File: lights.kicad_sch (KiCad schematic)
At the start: 0 parts

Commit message: Add Neopix
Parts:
- added C?: 1000uF, symbol Device:C
- added D? (x60): SK6812, LED_SMD:LED_SK6812_PLCC4_5.0x5.0mm_P3.2mm, symbol LED:SK6812
- added IC?: 74AHCT1G125DBVRG4, SOT95P280X145-5N, symbol JonasLib-Git:74AHCT1G125DBVRG4
- added R?: 100, symbol Device:R
- added R?: 470, symbol Device:R
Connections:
- new net: D?.2 (DIN), D?.4 (DOUT) (x59)
- new net: IC?.2 (A), R?.2
- new net: IC?.4 (Y), R?.1
- new net: D?.2 (DIN), R?.2
- new net GND: C?.2, D?.1 (VSS), D?.1 (VSS), D?.1 (VSS), D?.1 (VSS), D?.1 (VSS), D?.1 (VSS), D?.1 (VSS), D?.1 (VSS), D?.1 (VSS), D?.1 (VSS), D?.1 (VSS), D?.1 (VSS), D?.1 (VSS), D?.1 (VSS), D?.1 (VSS), D?.1 (VSS), D?.1 (VSS), D?.1 (VSS), D?.1 (VSS), D?.1 (VSS), D?.1 (VSS), D?.1 (VSS), D?.1 (VSS), D?.1 (VSS), D?.1 (VSS), D?.1 (VSS), D?.1 (VSS), D?.1 (VSS), D?.1 (VSS), D?.1 (VSS), D?.1 (VSS), D?.1 (VSS), D?.1 (VSS), D?.1 (VSS), D?.1 (VSS), D?.1 (VSS), D?.1 (VSS), D?.1 (VSS), D?.1 (VSS), D?.1 (VSS), D?.1 (VSS), D?.1 (VSS), D?.1 (VSS), D?.1 (VSS), D?.1 (VSS), D?.1 (VSS), D?.1 (VSS), D?.1 (VSS), D?.1 (VSS), D?.1 (VSS), D?.1 (VSS), D?.1 (VSS), D?.1 (VSS), D?.1 (VSS), D?.1 (VSS), D?.1 (VSS), D?.1 (VSS), D?.1 (VSS), D?.1 (VSS), D?.1 (VSS), IC?.1 (~{OE}), IC?.3 (GND)
- new net PC13: R?.1
- new net VBUS: C?.1, D?.3 (VDD), D?.3 (VDD), D?.3 (VDD), D?.3 (VDD), D?.3 (VDD), D?.3 (VDD), D?.3 (VDD), D?.3 (VDD), D?.3 (VDD), D?.3 (VDD), D?.3 (VDD), D?.3 (VDD), D?.3 (VDD), D?.3 (VDD), D?.3 (VDD), D?.3 (VDD), D?.3 (VDD), D?.3 (VDD), D?.3 (VDD), D?.3 (VDD), D?.3 (VDD), D?.3 (VDD), D?.3 (VDD), D?.3 (VDD), D?.3 (VDD), D?.3 (VDD), D?.3 (VDD), D?.3 (VDD), D?.3 (VDD), D?.3 (VDD), D?.3 (VDD), D?.3 (VDD), D?.3 (VDD), D?.3 (VDD), D?.3 (VDD), D?.3 (VDD), D?.3 (VDD), D?.3 (VDD), D?.3 (VDD), D?.3 (VDD), D?.3 (VDD), D?.3 (VDD), D?.3 (VDD), D?.3 (VDD), D?.3 (VDD), D?.3 (VDD), D?.3 (VDD), D?.3 (VDD), D?.3 (VDD), D?.3 (VDD), D?.3 (VDD), D?.3 (VDD), D?.3 (VDD), D?.3 (VDD), D?.3 (VDD), D?.3 (VDD), D?.3 (VDD), D?.3 (VDD), D?.3 (VDD), D?.3 (VDD), IC?.5 (VCC)

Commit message: Finalilize the Keybord Shematic
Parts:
- added D? (x2): SK6812, LED_SMD:LED_SK6812_PLCC4_5.0x5.0mm_P3.2mm, symbol LED:SK6812
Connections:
- net GND: now also D?.1 (VSS), D?.1 (VSS)
- net VBUS: now also D?.3 (VDD), D?.3 (VDD)
- net at D?.4 (DOUT): now also D?.2 (DIN)
- net PC13 renamed PA0
- new net: D?.2 (DIN), D?.4 (DOUT)
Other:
- note added: "62 Neopix - USB.2.0 Device max 6.40 mA per NeoPix ~ 10% Brightness"

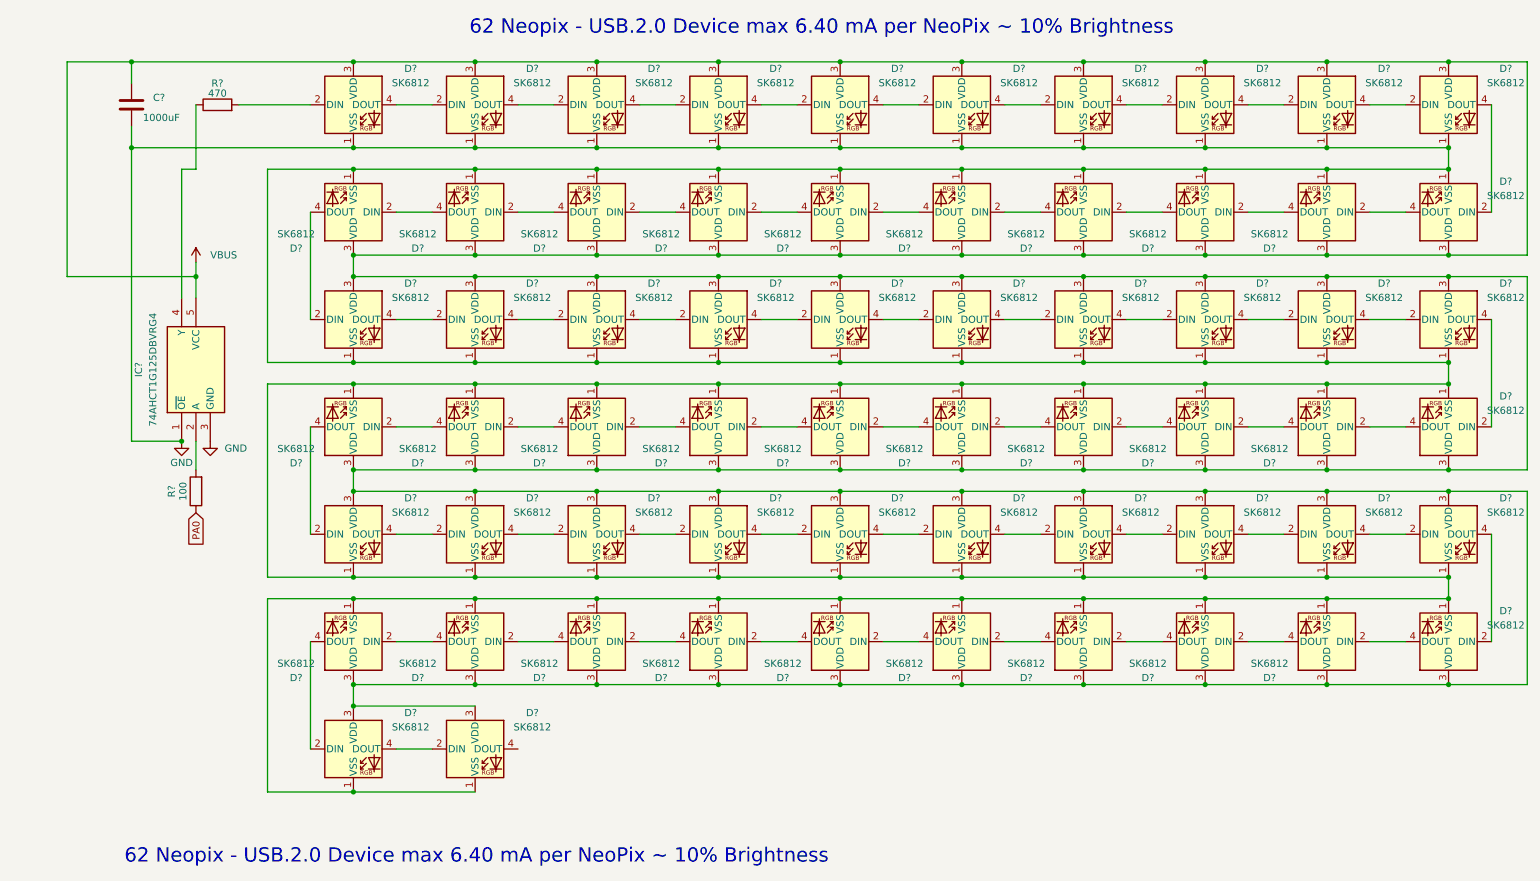
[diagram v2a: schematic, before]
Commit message: Start to fix ERC
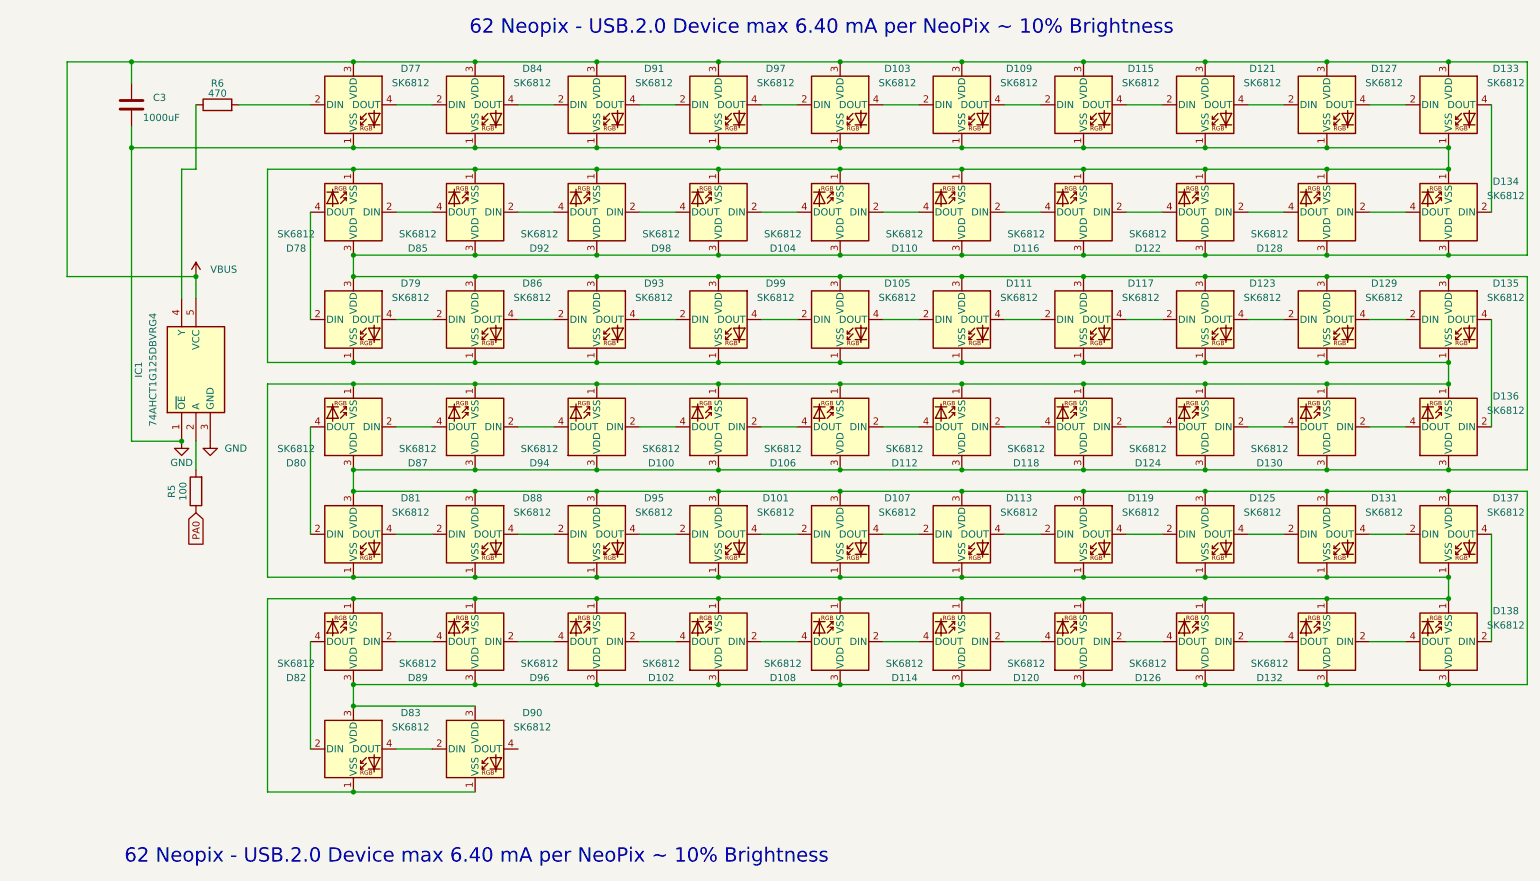
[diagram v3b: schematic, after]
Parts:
- IC1: renamed from IC?; footprint SOT95P280X145-5N -> JonasLib-Git:SOT95P280X145-5N
- gave numbers to parts that had none: 65

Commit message: Fixing. Add Footprints
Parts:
- C3: footprint (none) -> Capacitor_THT:C_Rect_L4.0mm_W2.5mm_P2.50mm
- R5, R6: footprint (none) -> Resistor_SMD:R_0603_1608Metric
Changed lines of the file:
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@@
 			)
 		)
-		(property "Footprint" ""
+		(property "Footprint" "Capacitor_THT:C_Rect_L4.0mm_W2.5mm_P2.50mm"
 			(at 27.6352 35.56 0)
 			(effects
@@
 			)
 		)
-		(property "Footprint" ""
+		(property "Footprint" "Resistor_SMD:R_0603_1608Metric"
 			(at 39.878 100.33 90)
 			(effects
@@
 			)
 		)
-		(property "Footprint" ""
+		(property "Footprint" "Resistor_SMD:R_0603_1608Metric"
 			(at 41.91 33.528 90)
 			(effects
